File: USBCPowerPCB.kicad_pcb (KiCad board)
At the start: 2 copper layers, 60 x 65 mm, 106 parts, among them IC2 TPS56A37RPAR, J1 USB_C_Receptacle_PowerOnly_6P, J10 GND_BANANA_OUT, J2 CC, J3 12V_OUT, J4 5V_ISO, J5 5V_OUT, J6 12V_OUT_PIN, J7 5V_ISO_PIN, J8 5V_OUT_PIN, J9 12V_BANANA_OUT, Q1 IRF9358TRPBF, Q2 BSL308PEH6327XTSA1, U1 TVS2200DRV, U2 CYPD3177-24LQXQT, U3 TPS562231DRLR, U4 TPS2116DRL, U5 TBA2-2411

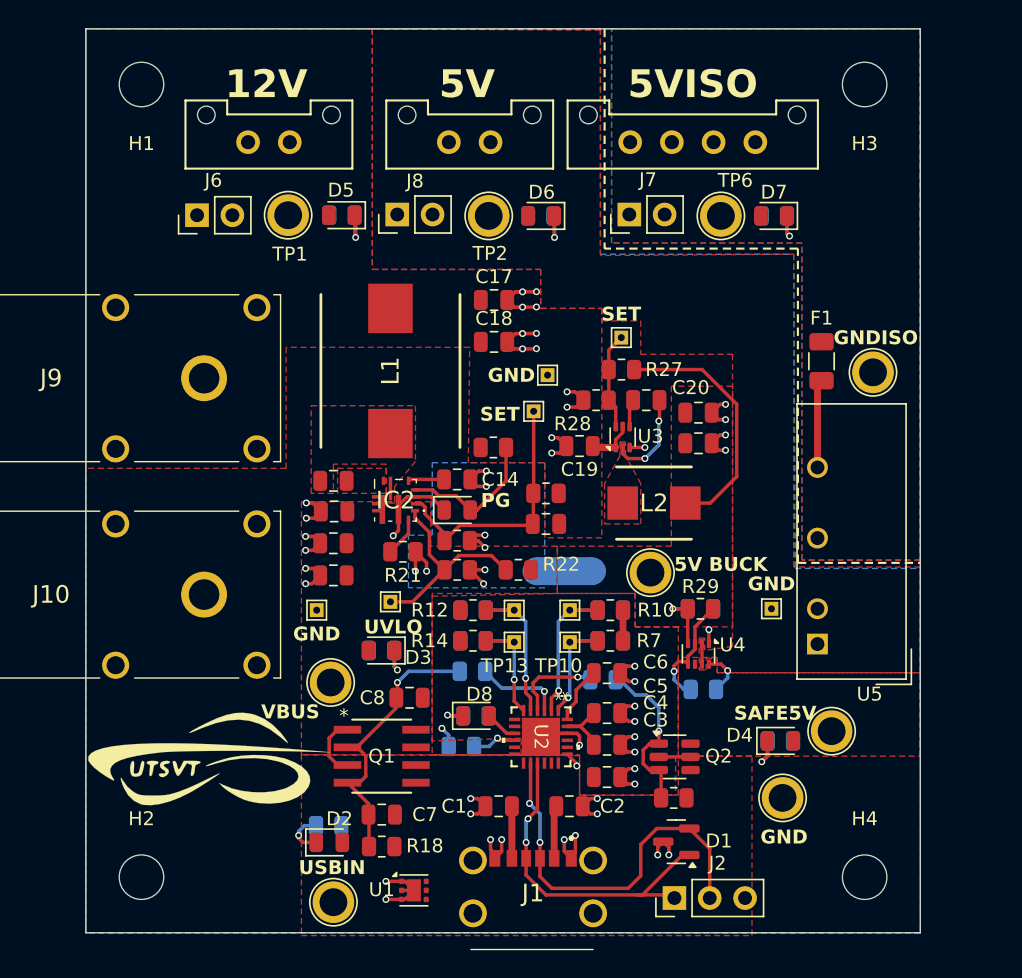
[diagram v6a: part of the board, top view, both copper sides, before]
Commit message: DRC passing: no warnings, no errors, no problem ✊🏿
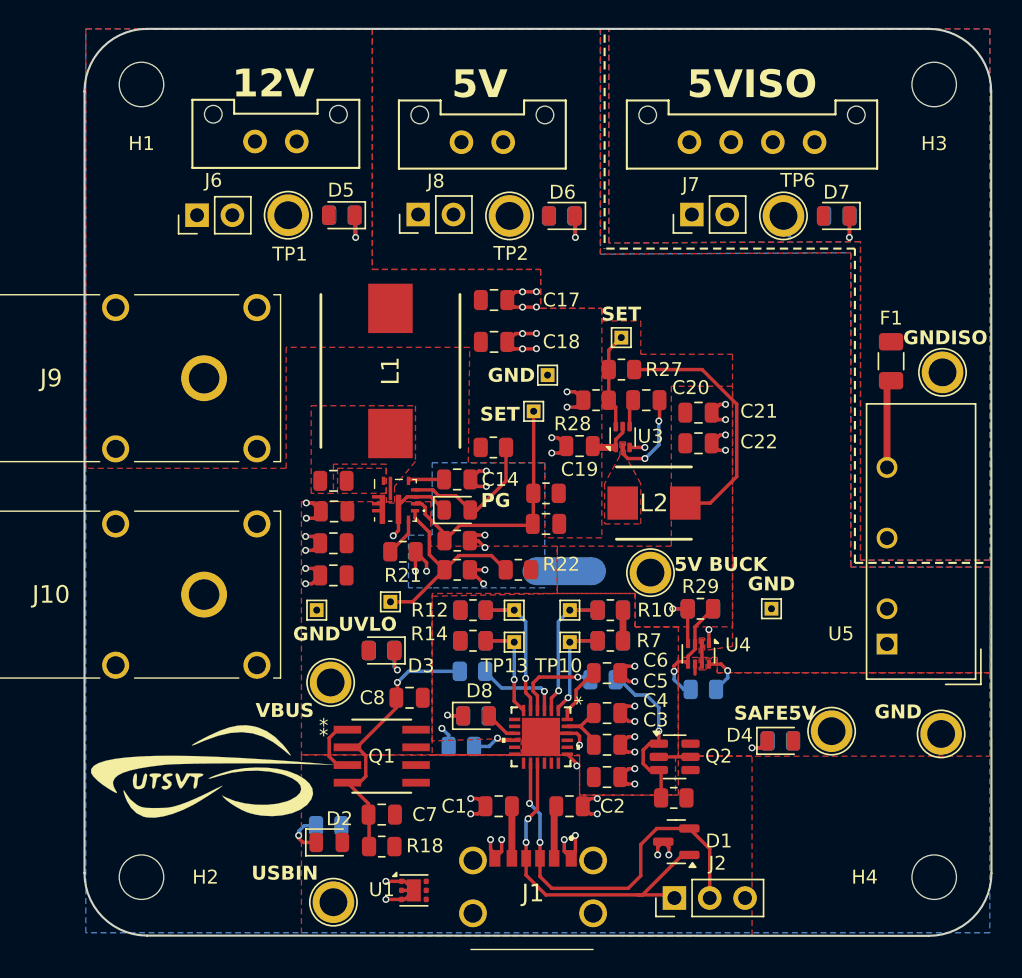
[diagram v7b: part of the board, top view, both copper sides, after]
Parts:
- added G***: LOGO, UTSVT_Special:Hallock_Image_Tiny, B.Cu at (117.8, 130.6)
- added G***: LOGO, UTSVT_Special:troll, B.Cu at (154.2, 104.4)
- moved TP19 12.3 mm to (171.6, 131.1)
- moved F1 5.00 mm to (168.0, 104.3)
- moved H3 5.00 mm to (171.1, 84.4)
- moved H4 5.00 mm to (171.1, 141.4)
- moved TP8 5.00 mm to (171.7, 105.1)
- moved U5 5.00 mm to (167.7, 124.6)
- moved D7 4.50 mm to (164.1, 93.8)
- moved J7 4.50 mm to (153.7, 93.8)
- moved R6 4.50 mm to (164.1, 93.8)
- moved TP6 4.50 mm to (160.3, 93.8)
- moved J4 4.26 mm to (153.5, 88.5)
- moved D6 1.50 mm to (144.3, 93.8)
- moved J8 1.50 mm to (134.0, 93.8)
- moved R5 1.50 mm to (144.3, 93.8)
- moved TP2 1.50 mm to (140.6, 93.8)
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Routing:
- net /5V_ISO: track 0.00 -> 1.54 mm
- net /SAFE_5V: track 0.00 -> 0.72 mm
- net Net-(D4-K): track 3.34 -> 2.64 mm
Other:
- board size 60 x 65 mm -> 65.2 x 65.2 mm
- board text added: "LHR Solar Ishan Deshpande"
- board text added: "USB Type-C Power Supply"

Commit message: done
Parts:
- L1: footprint UTSVT_Passive:INDPM110100X400N -> Inductor_SMD:L_Bourns_SRP1038C_10.0x10.0mm
- Q1: footprint UTSVT_ICs:SO8_IRF9358TRPBF_INF -> Package_SO:SO-8_3.9x4.9mm_P1.27mm
